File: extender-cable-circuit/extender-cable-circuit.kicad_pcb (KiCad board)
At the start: 4 copper layers, 64 x 86 mm, 81 parts, among them X3 24MHz

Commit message: Working on rally compact layout for cable extender.
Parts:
- removed C3: 100nF, Library:C0402
- moved FPC2 172.3 mm to (102.7, 88.4), turned to 90 degrees
- moved FPC4 172.0 mm to (103.2, 128.8), turned to 90 degrees
- moved USB2 163.6 mm to (107.0, 88.4), turned to 90 degrees
- moved USB4 163.3 mm to (107.6, 128.8), turned to 90 degrees
- moved R97 158.2 mm to (110.5, 92.6), turned to 90 degrees
- moved R20 156.6 mm to (112.0, 134.4), turned to 0 degrees
- moved R77 156.5 mm to (110.9, 90.0), turned to 90 degrees
- moved R81 155.7 mm to (112.1, 132.6), turned to 180 degrees
- moved R99 155.5 mm to (111.8, 130.4), turned to 180 degrees
- moved R104 154.0 mm to (112.7, 92.6), turned to 90 degrees
- moved D18 153.8 mm to (112.2, 127.5), turned to 0 degrees
- moved R106 153.6 mm to (112.0, 125.2), turned to 180 degrees
- moved R18 152.9 mm to (112.7, 89.9), turned to 90 degrees
- moved D14 150.9 mm to (113.0, 85.0), turned to 90 degrees
- moved C16 129.6 mm to (129.2, 78.0)
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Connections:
- C10 pad 2: 3V3A -> 3V3
- C12 pad 2: 3V3A -> 3V3
- C13 pad 2: 3V3A -> 3V3
- C15 pad 2: 5V -> VBUS
- C16 pad 2: 5V -> VBUS
- C17 pad 2: 5V -> VBUS
- C18 pad 2: 5V -> VBUS
- C20 pad 2: 5V -> VBUS
- C5 pad 2: 3V3A -> 3V3
- C7 pad 2: 3V3A -> 3V3
- C8 pad 2: 3V3 -> /3V3-before-filter
- L2 pad 1: 3V3 -> /3V3-before-filter
- L2 pad 2: 3V3A -> 3V3
- U1 pad 10: 3V3A -> 3V3
- U1 pad 29: 3V3A -> 3V3
- U1 pad 36: 3V3A -> 3V3
- U1 pad 5: 3V3A -> 3V3
- U23 pad 1: 5V -> VBUS
- U26 pad 1: 5V -> VBUS
- U28 pad 1: 5V -> VBUS
- U3 pad 1: 5V -> VBUS
- U3 pad 3: 5V -> VBUS
- U3 pad 5: 3V3 -> /3V3-before-filter
- U7 pad 1: 5V -> VBUS
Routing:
- net GND: track 0.00 -> 335.3 mm, vias 0 -> 34
- net VBUS: track 0.00 -> 148.2 mm, vias 0 -> 8
- net I2C_SDA: track 0.00 -> 141.9 mm, vias 0 -> 5
- net I2C_SCL: track 0.00 -> 134.8 mm, vias 0 -> 2
- net IN_USB_D-: track 0.00 -> 128.3 mm, vias 0 -> 3
- net IN_USB_D+: track 0.00 -> 125.2 mm, vias 0 -> 1
- net 3V3: track 0.00 -> 125.2 mm, vias 0 -> 12
- net SERVO1_NRST: track 0.00 -> 56.6 mm, vias 0 -> 8
- net SERVO1_BOOT0: track 0.00 -> 47.8 mm, vias 0 -> 2
- net /servo-usb-connector/VBUSx: track 0.00 -> 43.7 mm, vias 0 -> 2
- net USBDN4_D-: track 0.00 -> 35.2 mm, vias 0 -> 1
- net USBDN4_D+: track 0.00 -> 34.4 mm, vias 0 -> 1
- net USBDN3_D-: track 0.00 -> 31.6 mm, vias 0 -> 1
- net USBDN3_D+: track 0.00 -> 31.4 mm, vias 0 -> 1
- net SERVO4_BOOT0: track 0.00 -> 28.6 mm, vias 0 -> 1
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
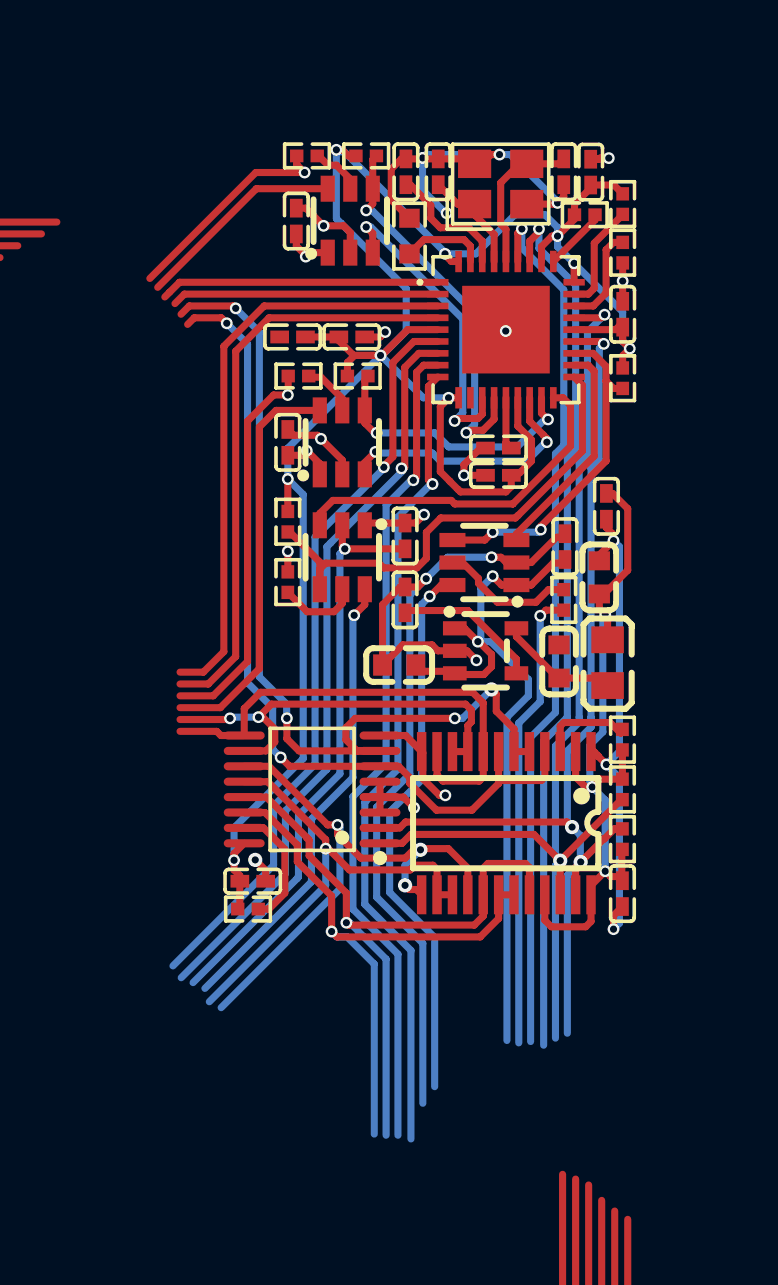
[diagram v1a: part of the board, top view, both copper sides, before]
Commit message: Sketch out output paths.
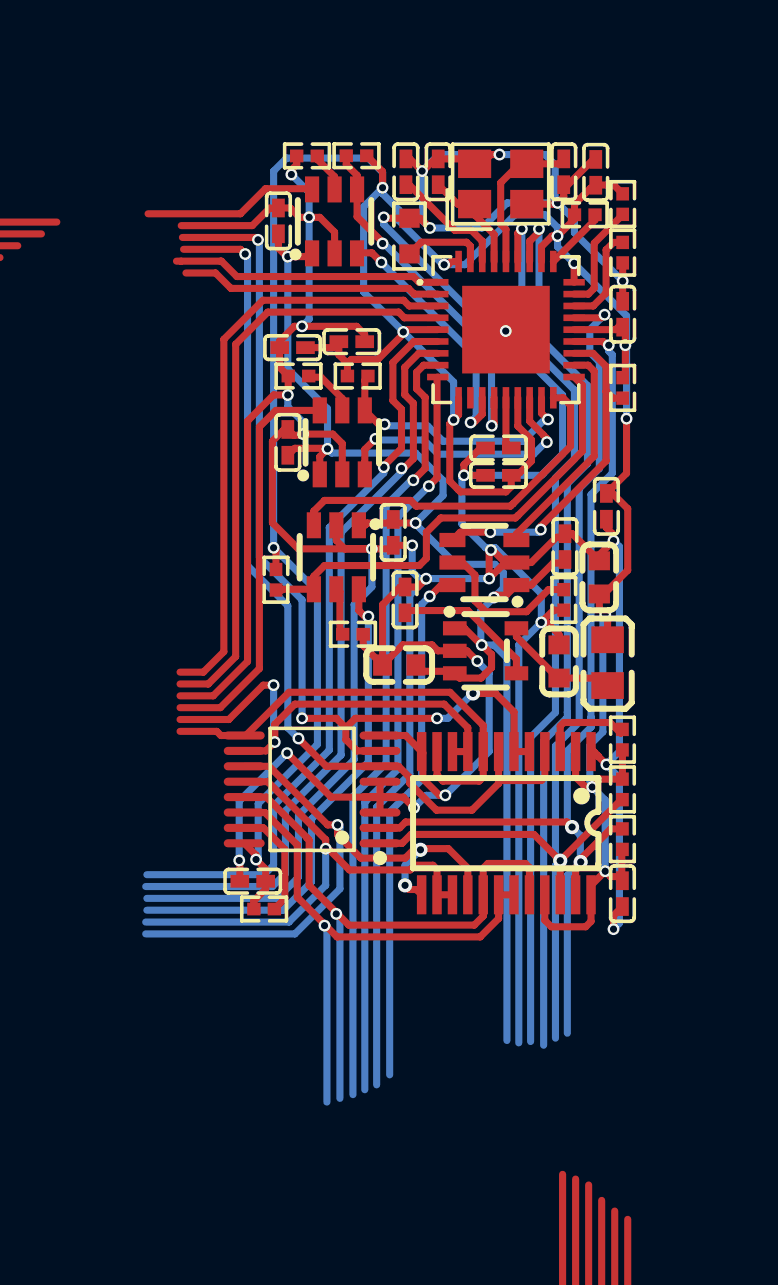
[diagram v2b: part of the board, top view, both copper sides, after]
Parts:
- moved R61 3.52 mm to (131.9, 86.2), turned to 180 degrees
- moved R82 2.50 mm to (128.7, 83.8)
- moved C15 0.75 mm to (128.8, 68.7)
- moved R4 0.68 mm to (128.2, 97.8)
- moved U7 0.66 mm to (131.2, 68.7)
- moved C17 0.52 mm to (133.7, 81.8)
- moved C10 0.45 mm to (129.4, 74.0)
- moved R79 0.41 mm to (132.1, 66.0), turned to 180 degrees
- moved R83 0.41 mm to (143.3, 75.8)
- moved U26 0.25 mm to (131.2, 82.9)
- moved C5 0.21 mm to (142.2, 66.7)
- moved C7 0.20 mm to (131.9, 73.8)
- turned C1 to 0 degrees
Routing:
- net GND: track 335.3 -> 418.2 mm, vias 34 -> 36
- net VBUS: track 148.2 -> 169.9 mm
- net 3V3: track 125.2 -> 138.8 mm, vias 12 -> 13
- net USBDN4_D+: track 34.4 -> 31.4 mm
- net SERVO1_BOOT0: track 47.8 -> 50.3 mm
- net PRTPWR1: track 13.3 -> 11.0 mm
- net USBDN4_D-: track 35.2 -> 33.0 mm
- net SERVO4_NRST: track 25.7 -> 23.8 mm
- net SERVO3_BOOT0: track 25.4 -> 27.3 mm
- net SERVO4_BOOT0: track 28.6 -> 26.8 mm
- net SERVO2_NRST: track 18.0 -> 19.7 mm
- net /servo-usb-connector/VBUSx: track 43.7 -> 42.2 mm
- net nOCS3: track 21.1 -> 19.6 mm
- net /servo-usb-connector2/VBUSx: track 19.6 -> 21.0 mm
- net /servo-usb-connector2/ILIMx: track 3.38 -> 2.04 mm
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
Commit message: Work on cable outline, and almost finish wiring.
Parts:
- moved FPC1 109.7 mm to (210.8, 59.2), turned to -90 degrees
- moved FPC3 108.9 mm to (210.8, 96.2), turned to -90 degrees
- moved FPC2 108.6 mm to (210.8, 77.8), turned to -90 degrees
- moved FPC4 108.5 mm to (210.8, 114.8), turned to -90 degrees
- moved R20 58.4 mm to (58.5, 111.1)
- moved R18 56.5 mm to (58.5, 74.1), turned to 0 degrees
- moved R98 55.9 mm to (58.9, 94.1), turned to 180 degrees
- moved R99 55.8 mm to (58.9, 112.6)
- moved R81 55.4 mm to (58.5, 118.5)
- moved R104 55.2 mm to (59.0, 80.0), turned to 180 degrees
- moved R105 55.1 mm to (59.0, 98.5), turned to 180 degrees
- moved USB4 55.0 mm to (54.4, 114.7)
- moved R19 55.0 mm to (58.5, 92.6), turned to 0 degrees
- moved D16 54.8 mm to (59.0, 96.3)
- moved USB3 54.7 mm to (54.4, 96.2)
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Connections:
- FPC0 pad 1: GND -> VCC
- FPC0 pad 10: GND -> VCC
- FPC0 pad 11: VCC -> GND
- FPC0 pad 12: VCC -> GND
- FPC0 pad 13: VCC -> GND
- FPC0 pad 14: VCC -> GND
- FPC0 pad 15: VCC -> GND
- FPC0 pad 16: VCC -> GND
- FPC0 pad 17: VCC -> GND
- FPC0 pad 18: VCC -> GND
- FPC0 pad 19: VCC -> GND
- FPC0 pad 2: GND -> VCC
- FPC0 pad 20: VCC -> GND
- FPC0 pad 3: GND -> VCC
- FPC0 pad 4: GND -> VCC
- FPC0 pad 5: GND -> VCC
- FPC0 pad 6: GND -> VCC
- FPC0 pad 7: GND -> VCC
- FPC0 pad 8: GND -> VCC
- FPC0 pad 9: GND -> VCC
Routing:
- net GND: track 418.2 -> 689.8 mm, vias 36 -> 47
- net /servo-usb-connector3/VBUSx: track 22.1 -> 116.1 mm, vias 1 -> 3
- net /servo-usb-connector2/VBUSx: track 21.0 -> 102.1 mm, vias 1 -> 4
- net SERVO4_NRST: track 23.8 -> 99.2 mm, vias 1 -> 4
- net USBDN4_D-: track 33.0 -> 108.3 mm, vias 1 -> 4
- net USBDN4_D+: track 31.4 -> 106.5 mm, vias 1 -> 2
- net SERVO4_BOOT0: track 26.8 -> 97.7 mm, vias 1 -> 2
- net USBDN3_D-: track 31.4 -> 100.4 mm, vias 1 -> 4
- net SERVO3_NRST: track 21.6 -> 88.2 mm, vias 1 -> 4
- net USBDN3_D+: track 31.6 -> 97.7 mm, vias 1 -> 2
- net /servo-usb-connector1/VBUSx: track 17.1 -> 82.9 mm, vias 0 -> 4
- net SERVO3_BOOT0: track 27.3 -> 89.6 mm, vias 3 -> 4
- net SERVO2_BOOT0: track 19.5 -> 79.1 mm, vias 0 -> 2
- net SERVO2_NRST: track 19.7 -> 74.0 mm, vias 2 -> 4
- net USBDN2_D-: track 25.2 -> 69.4 mm, vias 0 -> 2
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- removed copper zone on In2.Cu, net GND
- removed copper zone on In1.Cu, net VCC
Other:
- board size 64 x 86 mm -> 160 x 70 mm
- copper layers 4 -> 2
- board text added: "Stiffner 0.3mm total"

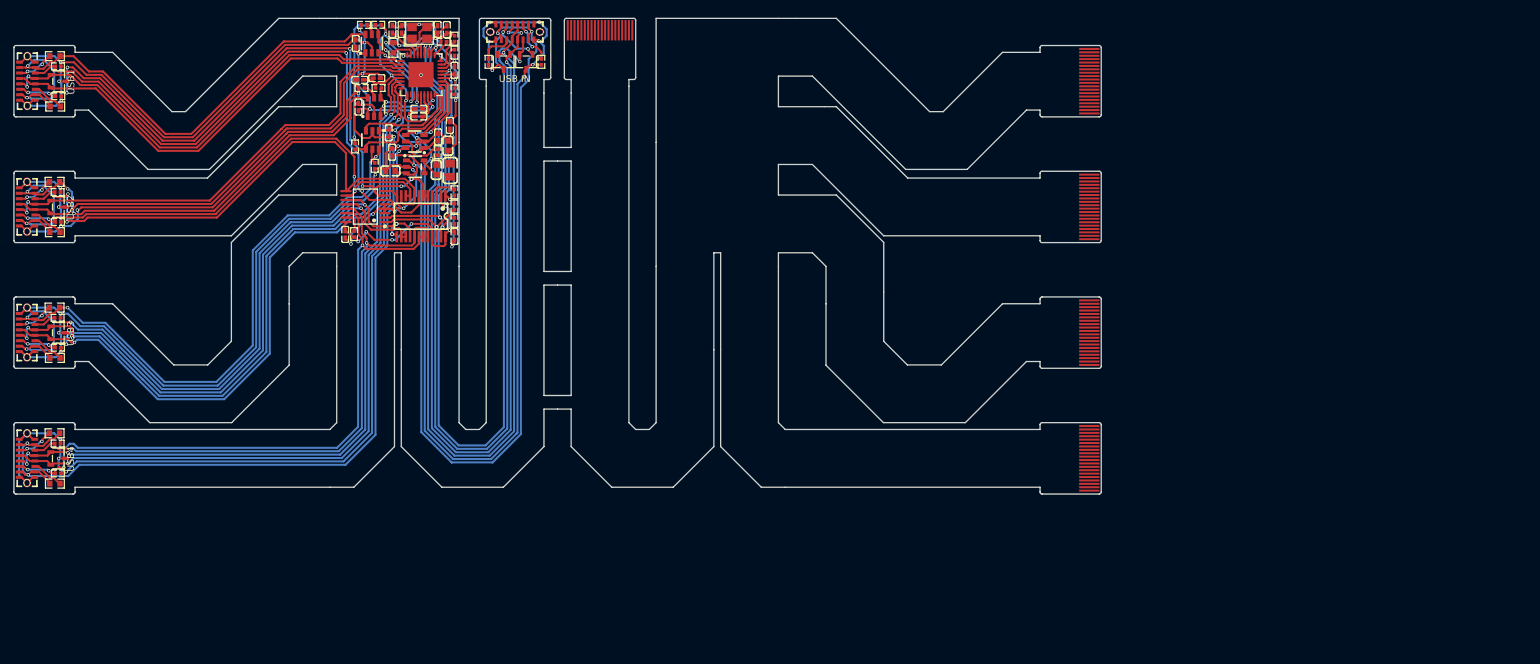
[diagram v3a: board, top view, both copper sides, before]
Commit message: Finish extender cable circuit.
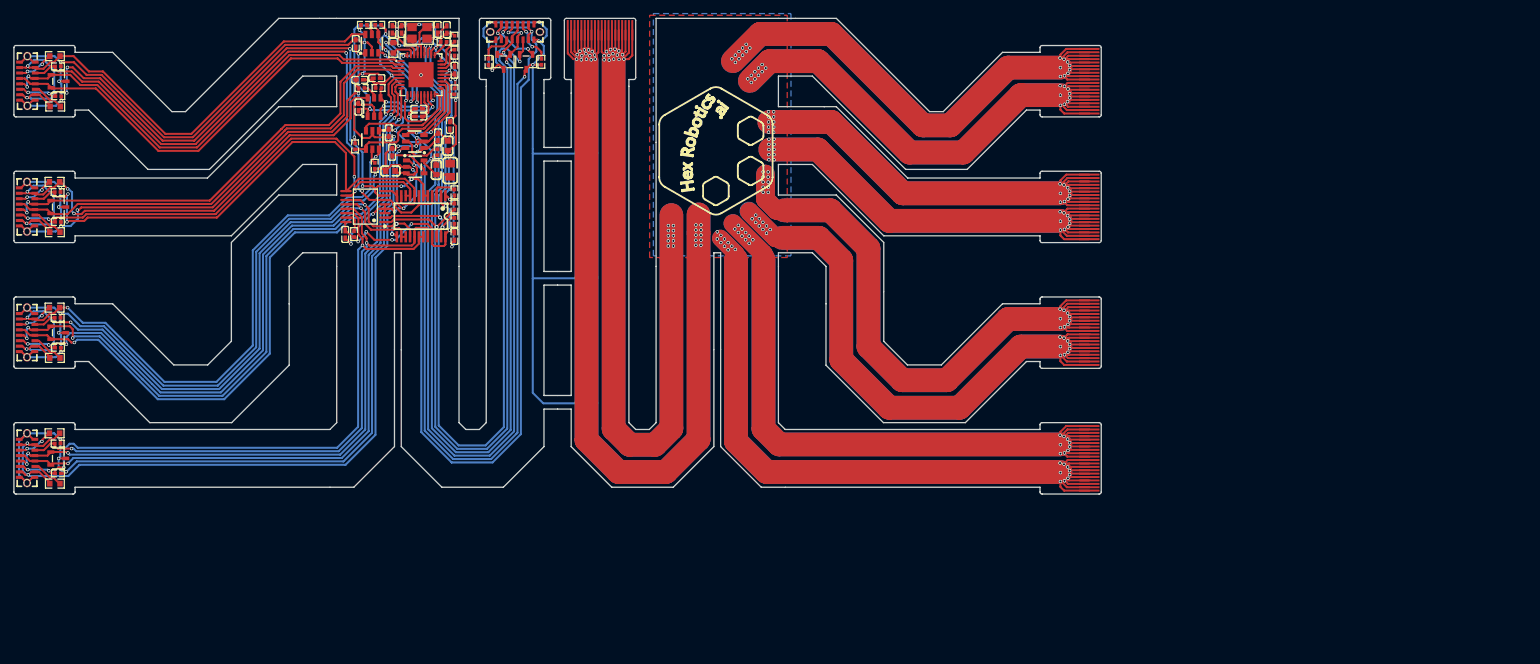
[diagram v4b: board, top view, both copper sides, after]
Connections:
- FPC0 pad 1: VCC -> GND
- FPC0 pad 10: VCC -> GND
- FPC0 pad 11: GND -> VCC
- FPC0 pad 12: GND -> VCC
- FPC0 pad 13: GND -> VCC
- FPC0 pad 14: GND -> VCC
- FPC0 pad 15: GND -> VCC
- FPC0 pad 16: GND -> VCC
- FPC0 pad 17: GND -> VCC
- FPC0 pad 18: GND -> VCC
- FPC0 pad 19: GND -> VCC
- FPC0 pad 2: VCC -> GND
- FPC0 pad 20: GND -> VCC
- FPC0 pad 3: VCC -> GND
- FPC0 pad 4: VCC -> GND
- FPC0 pad 5: VCC -> GND
- FPC0 pad 6: VCC -> GND
- FPC0 pad 7: VCC -> GND
- FPC0 pad 8: VCC -> GND
- FPC0 pad 9: VCC -> GND
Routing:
- net GND: track 689.8 -> 1740.6 mm, vias 47 -> 147
- net VCC: track 0.00 -> 953.3 mm, vias 0 -> 100
- added copper zone on B.Cu, net GND
- added copper zone on F.Cu, net VCC
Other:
- board text added: "VCC|GND"
